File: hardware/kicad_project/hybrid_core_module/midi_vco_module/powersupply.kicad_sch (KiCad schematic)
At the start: 64 parts, among them J10 Conn_01x06_Pin, J23 Conn_01x06_Pin, J9 Conn_02x08_Odd_Even, Q1 2N7002, U16 MC79M12CDTRKG, U3 USBLC6-2SC6, U4 TPS65131TRGERQ1, U5 MC78M12CDTRKG, U7 6N137, U8 AZ1117CH2-3.3

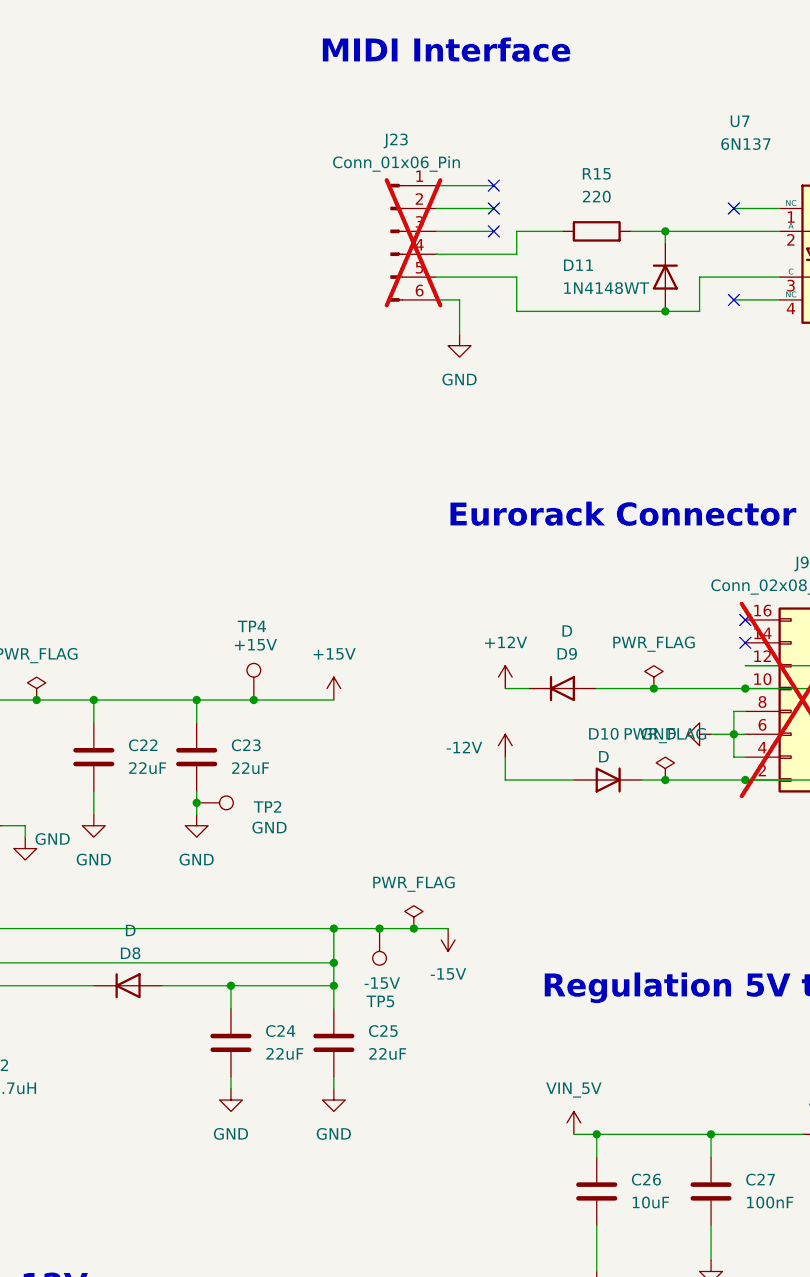
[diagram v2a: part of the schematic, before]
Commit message: components placement (interface) components placement per section
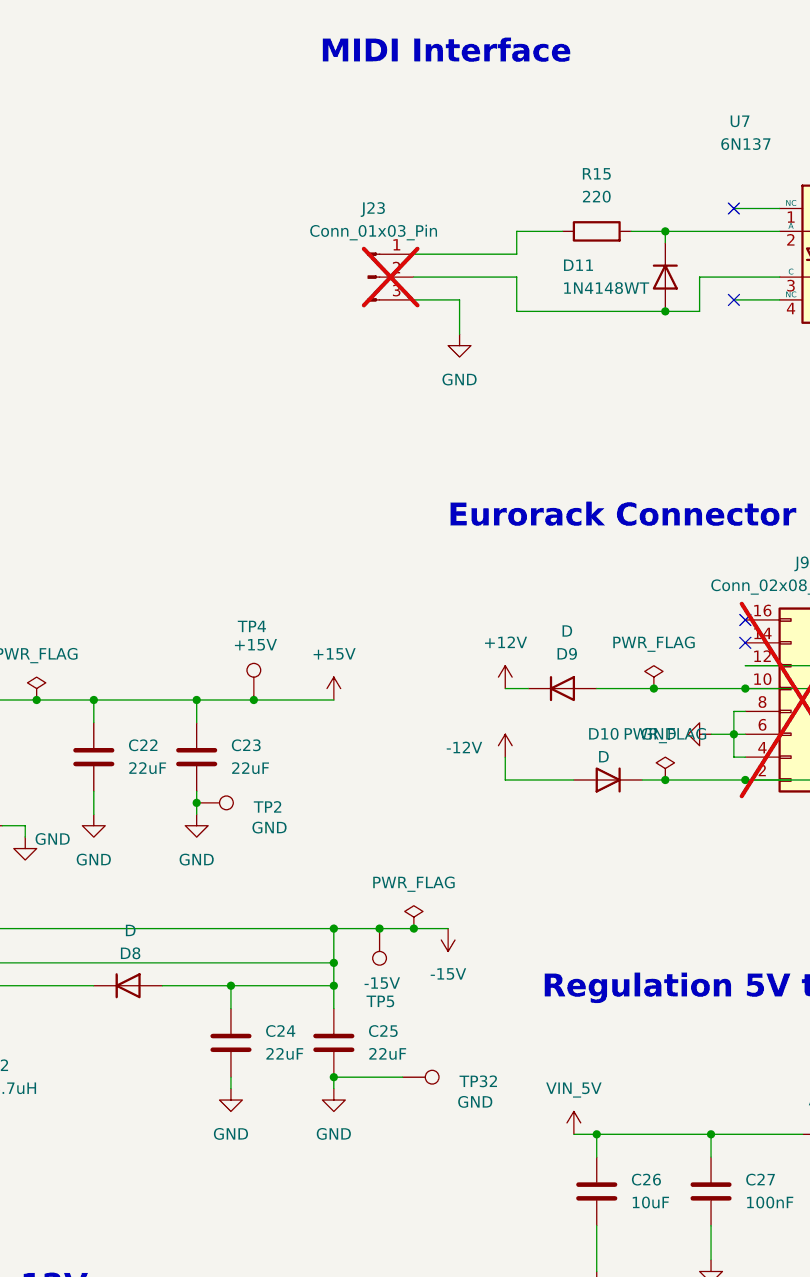
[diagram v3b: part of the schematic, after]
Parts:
- removed J23: Conn_01x06_Pin, Connector_PinHeader_1.00mm:PinHeader_1x01_P1.00mm_Vertical, symbol Connector:Conn_01x06_Pin
- added J23: Conn_01x03_Pin, Connector_PinHeader_2.54mm:PinHeader_1x03_P2.54mm_Vertical, symbol Connector:Conn_01x03_Pin
- added TP32: GND, TestPoint:TestPoint_Pad_1.0x1.0mm, symbol Connector:TestPoint
- J10: footprint Connector_PinHeader_1.00mm:PinHeader_1x01_P1.00mm_Vertical -> Connector_PinHeader_2.54mm:PinHeader_1x06_P2.54mm_Vertical
- R12: footprint Resistor_SMD:R_1206_3216Metric -> Resistor_SMD:R_0402_1005Metric; Manufacturer PartNumer RT1206FRE07976KL -> RC0402FR-07976KL
- R13: footprint Resistor_SMD:R_0805_2012Metric -> Resistor_SMD:R_0402_1005Metric; Manufacturer PartNumer RC0805FR-071M3L -> RC0402FR-071M3L
- R5: footprint Resistor_SMD:R_0402_1005Metric -> Resistor_SMD:R_1210_3225Metric
- TP1, TP2, TP3, TP4, TP5, TP6: footprint (none) -> TestPoint:TestPoint_Pad_1.0x1.0mm
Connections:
- net GND: now also J23.3 (Pin_3), TP32.1
- net at R15.1: now also J23.1 (Pin_1)
- net at D11.2 (A), U7.3 (C): now also J23.2 (Pin_2)
- no-connect marks 10 -> 7
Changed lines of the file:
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@@
 	)
 	(junction
+		(at 177.8 133.35)
+		(diameter 0)
+		(color 0 0 0 0)
+	)
+	(junction
 		(at 146.05 179.07)
 		(diameter 0)
@@
 	)
 	(no_connect
-		(at 195.58 39.37)
-	)
-	(no_connect
 		(at 236.22 85.09)
 	)
 	(no_connect
-		(at 195.58 34.29)
-	)
-	(no_connect
 		(at 236.22 82.55)
 	)
@@
 	)
 	(no_connect
-		(at 195.58 36.83)
-	)
-	(no_connect
 		(at 223.52 82.55)
 	)
@@
 	(wire
 		(pts
-			(xy 189.23 39.37) (xy 195.58 39.37)
-		)
-		(stroke
-			(width 0)
-			(type default)
-		)
-	)
-	(wire
-		(pts
 			(xy 196.85 100.33) (xy 196.85 97.79)
 		)
@@
 	(wire
 		(pts
-			(xy 189.23 41.91) (xy 198.12 41.91)
+			(xy 186.69 41.91) (xy 198.12 41.91)
 		)
 		(stroke
@@
 	(wire
 		(pts
-			(xy 189.23 36.83) (xy 195.58 36.83)
-		)
-		(stroke
-			(width 0)
-			(type default)
-		)
-	)
-	(wire
-		(pts
 			(xy 31.75 143.51) (xy 27.94 143.51)
 		)
@@
 	(wire
 		(pts
-			(xy 189.23 44.45) (xy 198.12 44.45)
+			(xy 186.69 44.45) (xy 198.12 44.45)
 		)
 		(stroke
@@
 	(wire
 		(pts
-			(xy 191.77 46.99) (xy 189.23 46.99)
+			(xy 191.77 46.99) (xy 186.69 46.99)
 		)
 		(stroke
@@
 	(wire
 		(pts
-			(xy 189.23 34.29) (xy 195.58 34.29)
+			(xy 185.42 133.35) (xy 177.8 133.35)
 		)
 		(stroke
@@
 			)
 		)
-		(property "Footprint" "Connector_PinHeader_1.00mm:PinHeader_1x01_P1.00mm_Vertical"
+		(property "Footprint" "Connector_PinHeader_2.54mm:PinHeader_1x06_P2.54mm_Vertical"
 			(at 26.67 46.99 0)
 			(effects
@@
 			)
 		)
-		(property "Footprint" ""
+		(property "Footprint" "TestPoint:TestPoint_Pad_1.0x1.0mm"
 			(at 85.09 175.26 0)
 			(effects
@@
 			)
 		)
-		(property "Footprint" ""
+		(property "Footprint" "TestPoint:TestPoint_Pad_1.0x1.0mm"
 			(at 162.56 107.95 0)
 			(effects
@@
 			)
 		)
-		(property "Footprint" ""
+		(property "Footprint" "TestPoint:TestPoint_Pad_1.0x1.0mm"
 			(at 173.99 91.44 0)
 			(effects
@@
 			)
 		)
-		(property "Footprint" "Resistor_SMD:R_0402_1005Metric"
+		(property "Footprint" "Resistor_SMD:R_1210_3225Metric"
 			(at 26.67 104.648 90)
 			(effects
@@
 			)
 		)
-		(property "Footprint" ""
+		(property "Footprint" "TestPoint:TestPoint_Pad_1.0x1.0mm"
 			(at 168.91 179.07 0)
 			(effects
@@
 			)
 		)
-		(property "Footprint" ""
+		(property "Footprint" "TestPoint:TestPoint_Pad_1.0x1.0mm"
 			(at 177.8 116.84 0)
 			(effects
@@
 			)
 		)
-		(property "Footprint" ""
+		(property "Footprint" "TestPoint:TestPoint_Pad_1.0x1.0mm"
 			(at 255.27 139.7 0)
 			(effects
@@
 			)
 		)
-		(property "Footprint" "Resistor_SMD:R_0805_2012Metric"
+		(property "Footprint" "Resistor_SMD:R_0402_1005Metric"
 			(at 128.27 115.062 90)
 			(effects
@@
 			)
 		)
-		(property "Manufacturer PartNumer" "RC0805FR-071M3L"
+		(property "Manufacturer PartNumer" "RC0402FR-071M3L"
 			(at 128.27 116.84 90)
 			(effects
@@
 	)
 	(symbol
+		(lib_id "Connector:Conn_01x03_Pin")
+		(at 181.61 44.45 0)
+		(unit 1)
+		(exclude_from_sim no)
+		(in_bom yes)
+		(on_board yes)
+		(dnp yes)
+		(fields_autoplaced yes)
+		(property "Reference" "J23"
+			(at 182.245 36.83 0)
+			(effects
+				(font
+					(size 1.27 1.27)
+				)
+			)
+		)
+		(property "Value" "Conn_01x03_Pin"
+			(at 182.245 39.37 0)
+			(effects
+				(font
+					(size 1.27 1.27)
+				)
+			)
+		)
+		(property "Footprint" "Connector_PinHeader_2.54mm:PinHeader_1x03_P2.54mm_Vertical"
+			(at 181.61 44.45 0)
+			(effects
+				(font
+					(size 1.27 1.27)
+				)
+				(hide yes)
+			)
+		)
+		(property "Datasheet" "~"
+			(at 181.61 44.45 0)
+			(effects
+				(font
+					(size 1.27 1.27)
+				)
+				(hide yes)
+			)
+		)
+		(property "Description" "Generic connector, single row, 01x03, script generated"
+			(at 181.61 44.45 0)
+			(effects
+				(font
+					(size 1.27 1.27)
+				)
+				(hide yes)
+			)
+		)
+		(pin "1"
+		)
+		(pin "3"
+		)
+		(pin "2"
+		)
+		(instances
+			(project ""
+				(path "/3378c2b5-f4b3-47f0-8cdf-dba4991b82b5/29afd42d-5315-4a67-91ab-a3c726b029f0"
+					(reference "J23")
+					(unit 1)
+				)
+			)
+		)
+	)
+	(symbol
 		(lib_id "Device:C")
 		(at 19.05 107.95 0)
@@
 	)
 	(symbol
+		(lib_id "Connector:TestPoint")
+		(at 185.42 133.35 270)
+		(unit 1)
+		(exclude_from_sim no)
+		(in_bom no)
+		(on_board yes)
+		(dnp no)
+		(property "Reference" "TP32"
+			(at 191.77 133.858 90)
+			(effects
+				(font
+					(size 1.27 1.27)
+				)
+				(justify left)
+			)
+		)
+		(property "Value" "GND"
+			(at 191.516 136.144 90)
+			(effects
+				(font
+					(size 1.27 1.27)
+				)
+				(justify left)
+			)
+		)
+		(property "Footprint" "TestPoint:TestPoint_Pad_1.0x1.0mm"
+			(at 185.42 138.43 0)
+			(effects
+				(font
+					(size 1.27 1.27)
+				)
+				(hide yes)
+			)
+		)
+		(property "Datasheet" "~"
+			(at 185.42 138.43 0)
+			(effects
+				(font
+					(size 1.27 1.27)
+				)
+				(hide yes)
+			)
+		)
+		(property "Description" "test point"
+			(at 185.42 133.35 0)
+			(effects
+				(font
+					(size 1.27 1.27)
+				)
+				(hide yes)
+			)
+		)
+		(property "MN" ""
+			(at 185.42 133.35 90)
+			(effects
+				(font
+					(size 1.27 1.27)
+				)
+				(hide yes)
+			)
+		)
+		(property "MPN" ""
+			(at 185.42 133.35 90)
+			(effects
+				(font
+					(size 1.27 1.27)
+				)
+				(hide yes)
+			)
+		)
+		(pin "1"
+		)
+		(instances
+			(project "midi_vco_module"
+				(path "/3378c2b5-f4b3-47f0-8cdf-dba4991b82b5/29afd42d-5315-4a67-91ab-a3c726b029f0"
+					(reference "TP32")
+					(unit 1)
+				)
+			)
+		)
+	)
+	(symbol
 		(lib_id "Device:C")
 		(at 58.42 123.19 0)
@@
 	)
 	(symbol
-		(lib_id "Connector:Conn_01x06_Pin")
-		(at 184.15 39.37 0)
-		(unit 1)
-		(exclude_from_sim no)
-		(in_bom yes)
-		(on_board yes)
-		(dnp yes)
-		(fields_autoplaced yes)
-		(property "Reference" "J23"
-			(at 184.785 29.21 0)
-			(effects
-				(font
-					(size 1.27 1.27)
-				)
-			)
-		)
-		(property "Value" "Conn_01x06_Pin"
-			(at 184.785 31.75 0)
-			(effects
-				(font
-					(size 1.27 1.27)
-				)
-			)
-		)
-		(property "Footprint" "Connector_PinHeader_1.00mm:PinHeader_1x01_P1.00mm_Vertical"
-			(at 184.15 39.37 0)
-			(effects
-				(font
-					(size 1.27 1.27)
-				)
-				(hide yes)
-			)
-		)
-		(property "Datasheet" "~"
-			(at 184.15 39.37 0)
-			(effects
-				(font
-					(size 1.27 1.27)
-				)
-				(hide yes)
-			)
-		)
-		(property "Description" "Generic connector, single row, 01x06, script generated"
-			(at 184.15 39.37 0)
-			(effects
-				(font
-					(size 1.27 1.27)
-				)
-				(hide yes)
-			)
-		)
-		(property "MN" ""
-			(at 184.15 39.37 0)
-			(effects
-				(font
-					(size 1.27 1.27)
-				)
-				(hide yes)
-			)
-		)
-		(property "MPN" ""
-			(at 184.15 39.37 0)
-			(effects
-				(font
-					(size 1.27 1.27)
-				)
-				(hide yes)
-			)
-		)
-		(pin "3"
-		)
-		(pin "1"
-		)
-		(pin "4"
-		)
-		(pin "2"
-		)
-		(pin "6"
-		)
-		(pin "5"
-		)
-		(instances
-			(project "midi_vco_module"
-				(path "/3378c2b5-f4b3-47f0-8cdf-dba4991b82b5/29afd42d-5315-4a67-91ab-a3c726b029f0"
-					(reference "J23")
-					(unit 1)
-				)
-			)
-		)
-	)
-	(symbol
 		(lib_id "power:GND")
 		(at 127 165.1 0)
@@
 			)
 		)
-		(property "Footprint" "Resistor_SMD:R_1206_3216Metric"
+		(property "Footprint" "Resistor_SMD:R_0402_1005Metric"
 			(at 124.968 97.79 90)
 			(effects
@@
 			)
 		)
-		(property "Manufacturer PartNumer" "RT1206FRE07976KL"
+		(property "Manufacturer PartNumer" "RC0402FR-07976KL"
 			(at 123.19 97.79 0)
 			(effects

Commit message: - placement done - routing 60%
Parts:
- removed U3: USBLC6-2SC6, Package_TO_SOT_SMD:SOT-23-6, symbol Power_Protection:USBLC6-2SC6
- added D35, D36, D37: ESD9B5.0ST5G, Diode_SMD:D_SOD-923, symbol Diode:ESD9B5.0ST5G
- U7: footprint Package_DIP:PowerIntegrations_SMD-8 -> Package_DIP:DIP-8_W7.62mm
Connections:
- net GND: now also D35.1 (A1), D36.1 (A1), D37.1 (A1)
- net VUSB1: now also D37.2 (A2)
- net CP_D_N: now reaches J10.4 (Pin_4)
- net CP_D_N: now also D36.2 (A2)
- net CP_D_P: now reaches J10.5 (Pin_5)
- net CP_D_P: now also D35.2 (A2)
- net INP: now reaches D4.2 (A), L1.2, U4.1 (INP), U4.24 (INP)
- net OUTN: now reaches D8.1 (K), L2.1, U4.13 (OUTN), U4.14 (OUTN)
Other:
- moved on the sheet: R10, R9
